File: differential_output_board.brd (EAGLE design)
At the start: 100 x 50 mm, 34 parts, among them IC1 TJA1057

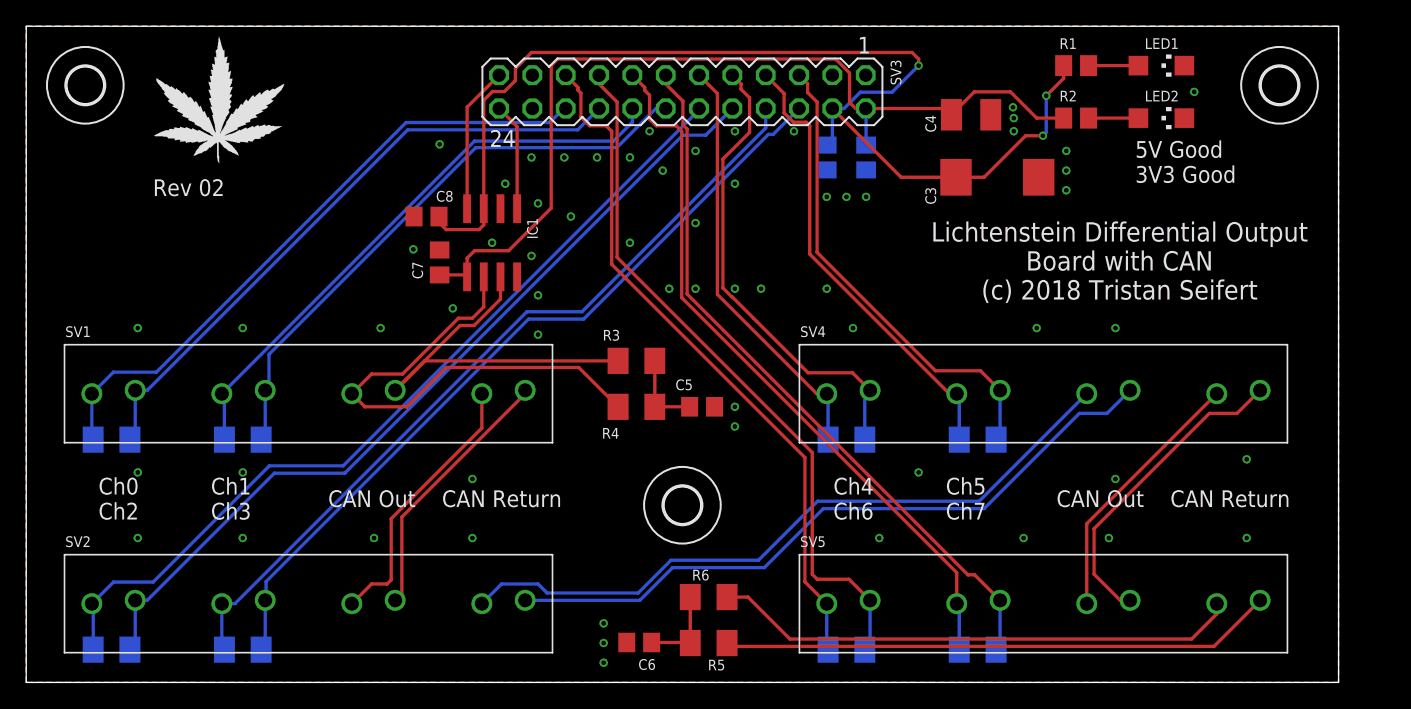
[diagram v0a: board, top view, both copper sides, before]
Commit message: removed input connector, cleaned up some signals
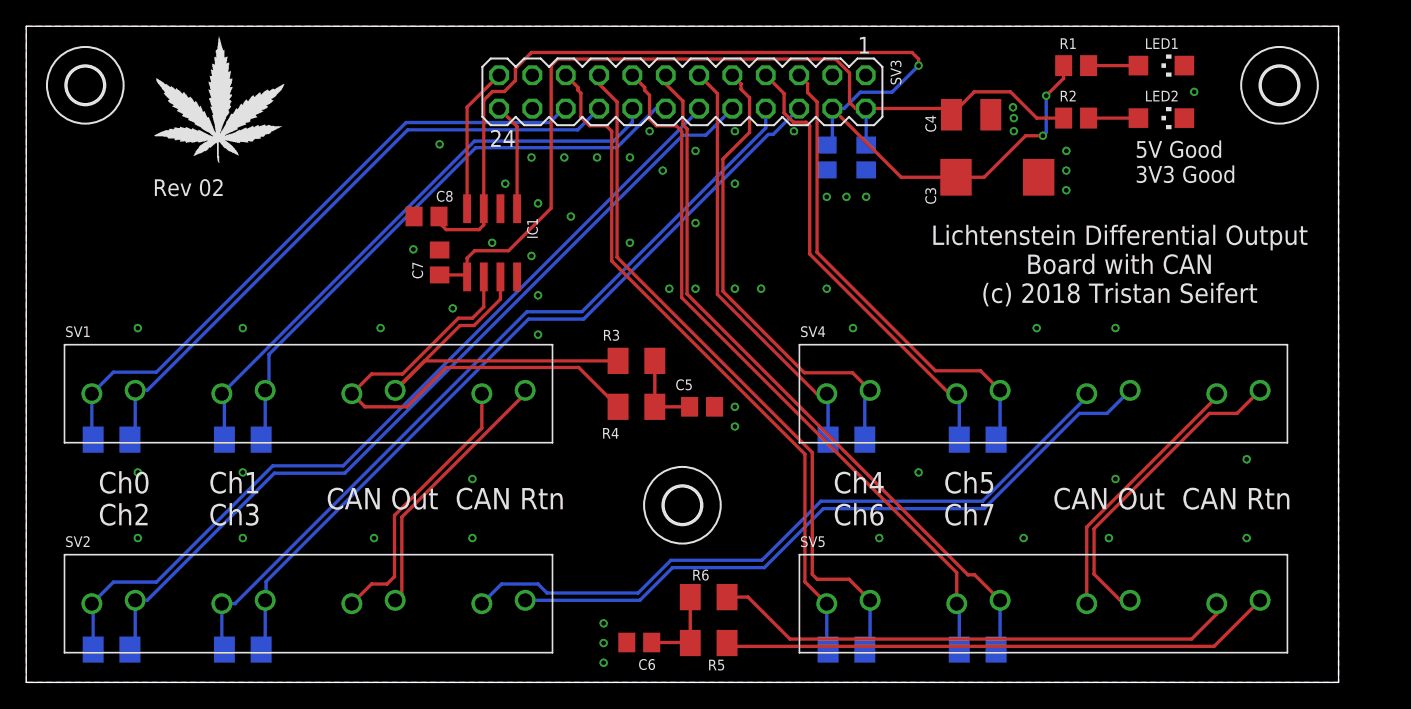
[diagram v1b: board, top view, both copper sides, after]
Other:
- board text added: "CAN Out CAN Rtn"
- board text removed: "CAN Out CAN Return"
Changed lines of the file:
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@@
 <wire x1="100" y1="50" x2="0" y2="50" width="0" layer="20"/>
 <wire x1="0" y1="50" x2="0" y2="0" width="0" layer="20"/>
-<text x="5.5" y="14" size="1.27" layer="25" font="vector" ratio="12" align="center-left">Ch0           Ch1
-Ch2           Ch3</text>
-<text x="61.5" y="14" size="1.27" layer="25" font="vector" ratio="12" align="center-left">Ch4           Ch5
-Ch6           Ch7</text>
-<text x="83.31" y="29.174" size="1.4732" layer="25" font="vector" ratio="12" align="bottom-center">Lichtenstein Differential Output
+<text x="5.5" y="14" size="1.6256" layer="25" font="vector" ratio="12" align="center-left">Ch0       Ch1
+Ch2       Ch3</text>
+<text x="61.5" y="14" size="1.6256" layer="25" font="vector" ratio="12" align="center-left">Ch4       Ch5
+Ch6       Ch7</text>
+<text x="83.31" y="28.92" size="1.4732" layer="25" font="vector" ratio="12" align="bottom-center">Lichtenstein Differential Output
 Board with CAN
 (c) 2018 Tristan Seifert</text>
 <text x="84.5" y="41.25" size="1.27" layer="25" font="vector" ratio="10" align="top-left">5V Good
 3V3 Good</text>
-<text x="23" y="14" size="1.27" layer="25" font="vector" ratio="12" align="center-left">CAN Out    CAN Return</text>
-<text x="78.5" y="14" size="1.27" layer="25" font="vector" ratio="12" align="center-left">CAN Out    CAN Return</text>
+<text x="22.86" y="14" size="1.6256" layer="25" font="vector" ratio="12" align="center-left">CAN Out  CAN Rtn</text>
+<text x="78.232" y="14" size="1.6256" layer="25" font="vector" ratio="12" align="center-left">CAN Out  CAN Rtn</text>
 <text x="9.65" y="38.334" size="1.27" layer="25" font="vector" ratio="10" align="top-left">Rev 02</text>
 </plain>
@@
 <wire x1="51.27" y1="43.73" x2="51.27" y2="43.62109375" width="0.254" layer="16"/>
 <wire x1="51.27" y1="43.62109375" x2="24.1503625" y2="16.50145625" width="0.254" layer="16"/>
-<wire x1="24.1503625" y1="16.50145625" x2="18.52550625" y2="16.50145625" width="0.254" layer="16"/>
-<wire x1="18.52550625" y1="16.50145625" x2="9.6663375" y2="7.6422875" width="0.254" layer="16"/>
-<wire x1="9.6663375" y1="7.6422875" x2="6.6422875" y2="7.6422875" width="0.254" layer="16"/>
+<wire x1="24.1503625" y1="16.50145625" x2="18.77950625" y2="16.50145625" width="0.254" layer="16"/>
+<wire x1="18.77950625" y1="16.50145625" x2="9.9203375" y2="7.6422875" width="0.254" layer="16"/>
+<wire x1="9.9203375" y1="7.6422875" x2="6.6422875" y2="7.6422875" width="0.254" layer="16"/>
 <wire x1="6.6422875" y1="7.6422875" x2="5" y2="6" width="0.254" layer="16"/>
 <contactref element="R9" pad="1"/>
@@
 <contactref element="SV5" pad="1"/>
 <wire x1="61" y1="6" x2="59.3363" y2="7.6637" width="0.254" layer="1"/>
-<wire x1="59.3363" y1="7.6637" x2="59.3363" y2="17.137525" width="0.254" layer="1"/>
-<wire x1="59.3363" y1="17.137525" x2="44.61539375" y2="31.85843125" width="0.254" layer="1"/>
+<wire x1="59.3363" y1="7.6637" x2="59.3363" y2="17.391525" width="0.254" layer="1"/>
+<wire x1="59.3363" y1="17.391525" x2="44.61539375" y2="32.11243125" width="0.254" layer="1"/>
 <wire x1="42.047553125" y1="45.115425" x2="42.264575" y2="44.898403125" width="0.254" layer="1"/>
 <wire x1="42.047553125" y1="45.115425" x2="42.047553125" y2="45.332446875" width="0.254" layer="1"/>
@@
 <wire x1="42.264575" y1="43.079425" x2="42.926" y2="42.418" width="0.254" layer="1"/>
 <wire x1="42.926" y1="42.418" x2="44.196" y2="42.418" width="0.254" layer="1"/>
-<wire x1="44.61539375" y1="41.99860625" x2="44.61539375" y2="31.85843125" width="0.254" layer="1"/>
+<wire x1="44.61539375" y1="41.99860625" x2="44.61539375" y2="32.11243125" width="0.254" layer="1"/>
 </signal>
 <signal name="OUT5_P">
 <contactref element="SV3" pad="9"/>
 <contactref element="SV4" pad="2"/>
-<wire x1="64.302" y1="22.254" x2="62.961615625" y2="23.594384375" width="0.254" layer="1"/>
-<wire x1="59.577971875" y1="23.594384375" x2="62.961615625" y2="23.594384375" width="0.254" layer="1"/>
-<wire x1="55.435809375" y1="27.736546875" x2="55.683178125" y2="27.489178125" width="0.254" layer="1"/>
-<wire x1="55.683178125" y1="27.489178125" x2="59.577971875" y2="23.594384375" width="0.254" layer="1"/>
+<wire x1="62.961615625" y1="23.594384375" x2="64.302" y2="22.254" width="0.254" layer="1"/>
 <wire x1="54.465021875" y1="45.614978125" x2="54.465021875" y2="45.198859375" width="0.254" layer="1"/>
 <wire x1="54.465021875" y1="45.614978125" x2="53.81" y2="46.27" width="0.254" layer="1"/>
@@
 <wire x1="54.465021875" y1="45.198859375" x2="55.118" y2="44.54588125" width="0.254" layer="1"/>
 <wire x1="55.118" y1="41.91" x2="53.086" y2="39.878" width="0.254" layer="1"/>
-<wire x1="53.74865" y1="29.3932" x2="53.77915625" y2="29.3932" width="0.254" layer="1"/>
-<wire x1="53.77915625" y1="29.3932" x2="55.435809375" y2="27.736546875" width="0.254" layer="1"/>
-<wire x1="53.086" y1="39.878" x2="53.086" y2="30.05585" width="0.254" layer="1"/>
-<wire x1="53.086" y1="30.05585" x2="53.74865" y2="29.3932" width="0.254" layer="1"/>
+<wire x1="53.086" y1="39.878" x2="53.086" y2="29.80185" width="0.254" layer="1"/>
 <wire x1="55.118" y1="44.54588125" x2="55.118" y2="41.91" width="0.254" layer="1"/>
+<wire x1="53.086" y1="29.80185" x2="59.293465625" y2="23.594384375" width="0.254" layer="1"/>
+<wire x1="59.293465625" y1="23.594384375" x2="62.961615625" y2="23.594384375" width="0.254" layer="1"/>
 </signal>
 <signal name="+5V">
@@
 <wire x1="24.812" y1="6" x2="26.312" y2="7.5" width="0.254" layer="1"/>
 <wire x1="26.312" y1="7.5" x2="27.5" y2="7.5" width="0.254" layer="1"/>
-<wire x1="27.5" y1="7.5" x2="27.8092" y2="7.8092" width="0.254" layer="1"/>
-<wire x1="27.8092" y1="7.8092" x2="27.8092" y2="12.47425625" width="0.254" layer="1"/>
+<wire x1="27.5" y1="7.5" x2="28.0632" y2="8.0632" width="0.254" layer="1"/>
+<wire x1="28.0632" y1="8.0632" x2="28.0632" y2="12.72825625" width="0.254" layer="1"/>
 <wire x1="34.718" y1="19.38305625" x2="34.718" y2="22" width="0.254" layer="1"/>
-<wire x1="27.8092" y1="12.47425625" x2="34.718" y2="19.38305625" width="0.254" layer="1"/>
+<wire x1="28.0632" y1="12.72825625" x2="34.718" y2="19.38305625" width="0.254" layer="1"/>
 </signal>
 <signal name="CANH_2">
@@
 <contactref element="SV2" pad="7"/>
 <contactref element="SV4" pad="5"/>
-<wire x1="60.2968" y1="13.8048" x2="55.7968" y2="9.3048" width="0.254" layer="16"/>
+<wire x1="60.5508" y1="13.8048" x2="56.0508" y2="9.3048" width="0.254" layer="16"/>
 <wire x1="49.11974375" y1="9.3048" x2="46.62774375" y2="6.8128" width="0.254" layer="16"/>
-<wire x1="55.7968" y1="9.3048" x2="49.11974375" y2="9.3048" width="0.254" layer="16"/>
+<wire x1="56.0508" y1="9.3048" x2="49.11974375" y2="9.3048" width="0.254" layer="16"/>
 <wire x1="39.6872" y1="6.8128" x2="39" y2="7.5" width="0.254" layer="16"/>
 <wire x1="39" y1="7.5" x2="36.218" y2="7.5" width="0.254" layer="16"/>
 <wire x1="36.218" y1="7.5" x2="34.718" y2="6" width="0.254" layer="16"/>
-<wire x1="80.812" y1="22" x2="72.6168" y2="13.8048" width="0.254" layer="16"/>
-<wire x1="72.6168" y1="13.8048" x2="60.2968" y2="13.8048" width="0.254" layer="16"/>
+<wire x1="80.812" y1="22" x2="80.812" y2="21.746" width="0.254" layer="16"/>
+<wire x1="80.812" y1="21.746" x2="72.8708" y2="13.8048" width="0.254" layer="16"/>
+<wire x1="72.8708" y1="13.8048" x2="60.5508" y2="13.8048" width="0.254" layer="16"/>
 <wire x1="46.62774375" y1="6.8128" x2="39.6872" y2="6.8128" width="0.254" layer="16"/>
 </signal>
@@
 <contactref element="SV4" pad="7"/>
 <contactref element="SV5" pad="5"/>
-<wire x1="90.718" y1="22" x2="80.812" y2="12.094" width="0.254" layer="1"/>
-<wire x1="80.812" y1="12.094" x2="80.812" y2="6" width="0.254" layer="1"/>
+<wire x1="90.718" y1="22" x2="90.718" y2="21.746" width="0.254" layer="1"/>
+<wire x1="90.718" y1="21.746" x2="80.812" y2="11.84" width="0.254" layer="1"/>
+<wire x1="80.812" y1="11.84" x2="80.812" y2="6" width="0.254" layer="1"/>
 </signal>
 <signal name="N$13">
